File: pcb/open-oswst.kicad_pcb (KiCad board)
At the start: 2 copper layers, 70 x 50 mm, 16 parts

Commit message: PCB: standardize all JST connectors on 2mm PH pitch
SPK was JST-ZH (1.5mm); now JST-PH (2.0mm) like all others.
Increased CHNL→SPK spacing to 10mm to fit wider housing.
Removed unused add_jst_sh and add_jst_zh from kicad.py.

Co-Authored-By: Claude Opus 4.6 <noreply@anthropic.com>
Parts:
- removed the SPK at (172.0, 118.0)
- added SPK: , JST_PH_B2B, F.Cu at (175.0, 118.0)
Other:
- board text added: "open-oswst 5c44884"
- board text removed: "open-oswst cabc854"
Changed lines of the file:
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@@
   )
   (gr_rect (start 113 113) (end 183 163) (stroke (width 0.1) (type solid)) (fill none) (layer "Edge.Cuts"))
-  (gr_text "open-oswst  cabc854"
+  (gr_text "open-oswst  5c44884"
     (at 148.0 161)
     (layer "F.SilkS")
@@
     )
   )
-  (footprint "JST_ZH_B2B"
-    (layer "F.Cu")
-    (at 172 118)
+  (footprint "JST_PH_B2B"
+    (layer "F.Cu")
+    (at 175 118)
     (fp_text reference "SPK" (at 0 -2.5) (layer "F.SilkS")
       (effects (font (size 1 1) (thickness 0.15)))
     )
     (pad "-" thru_hole circle
-      (at -0.75 0)
-      (size 1.1 1.1)
-      (drill 0.7)
+      (at -1.0 0)
+      (size 1.5 1.5)
+      (drill 0.8)
       (layers *.Cu *.Mask)
       (net 11 "SPK-")
     )
     (pad "+" thru_hole circle
-      (at 0.75 0)
-      (size 1.1 1.1)
-      (drill 0.7)
+      (at 1.0 0)
+      (size 1.5 1.5)
+      (drill 0.8)
       (layers *.Cu *.Mask)
       (net 12 "SPK+")

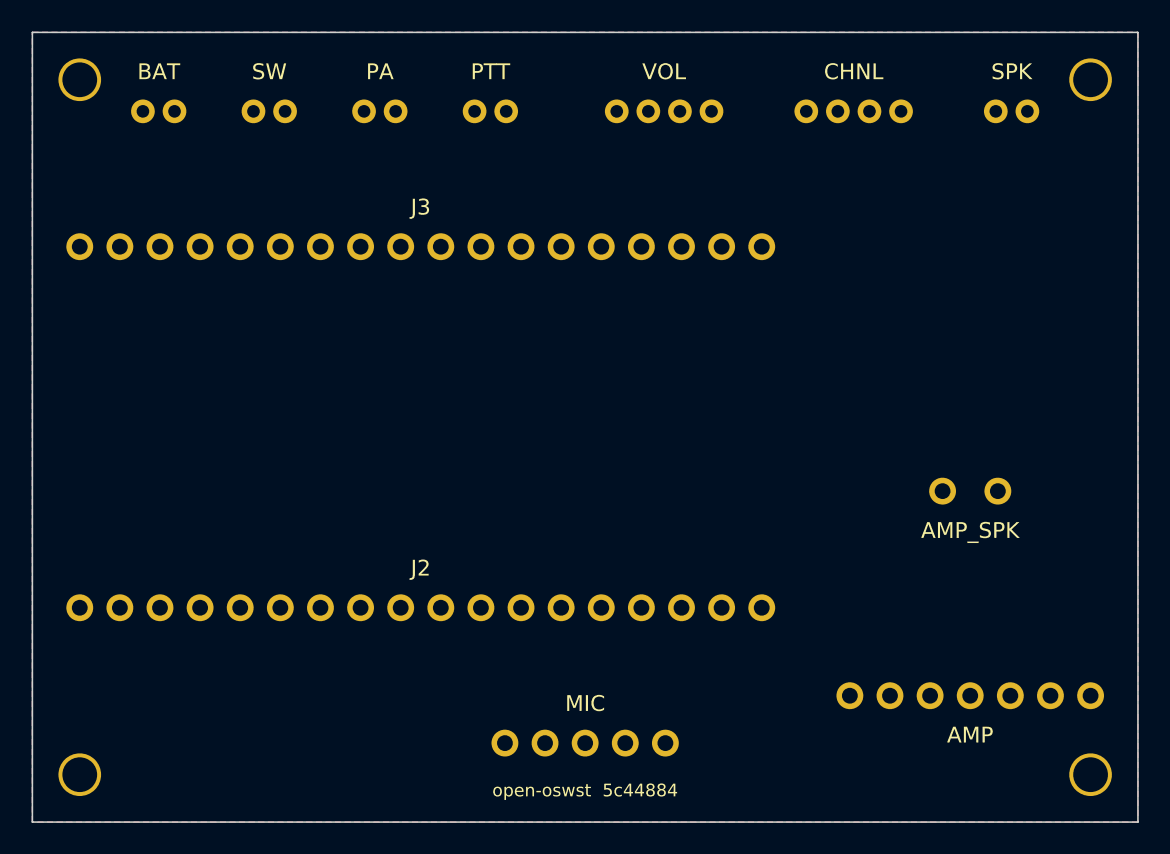
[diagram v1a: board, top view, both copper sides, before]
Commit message: PCB: match drill holes to case, relayout top connectors, move SPK to right edge
Mounting holes changed from 3mm uniform inset to 5mm LR / 2.5mm TB to
match existing case perfboard posts (60x45mm pattern). Top-edge connectors
shifted right and tightened (PTT→VOL 10mm, VOL→CHNL 11mm). SPK moved to
right edge (rotated 90°) to free space. Removed unused JST-SH/ZH methods.

Co-Authored-By: Claude Opus 4.6 <noreply@anthropic.com>
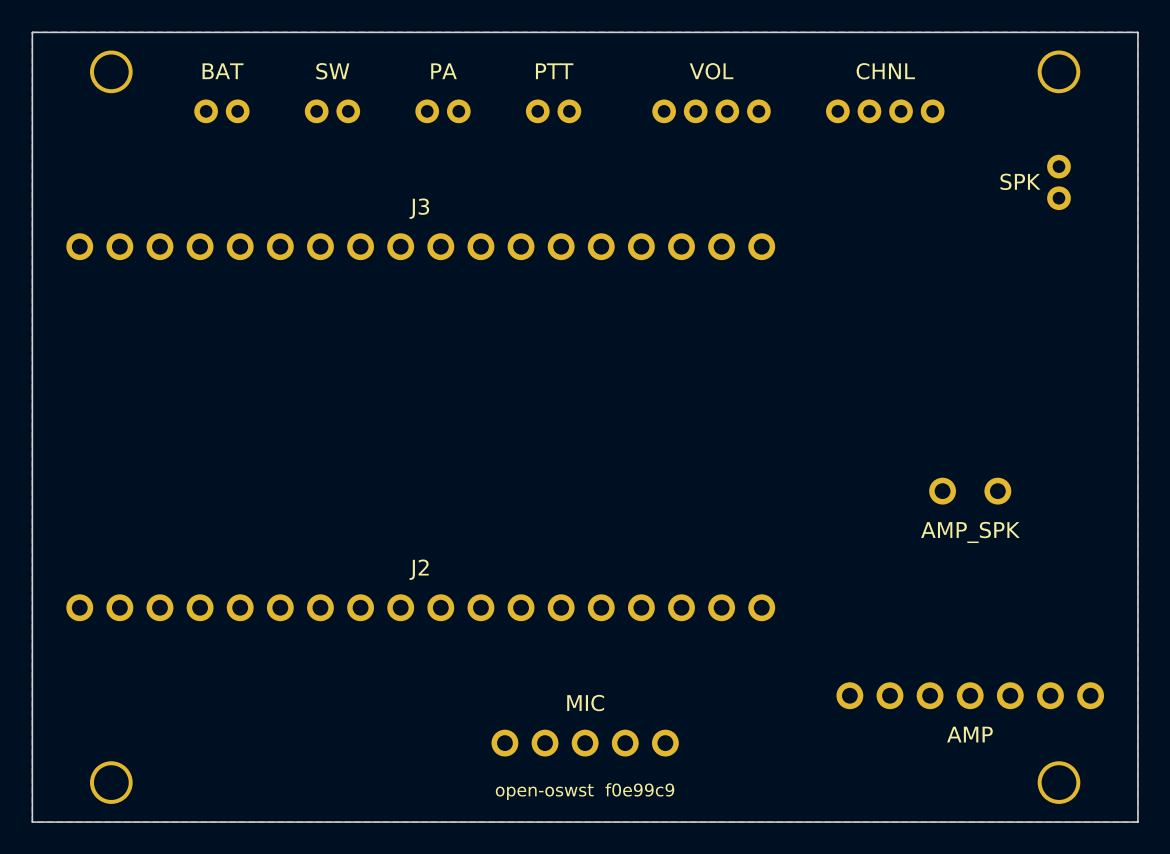
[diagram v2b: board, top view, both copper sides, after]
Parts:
- moved SPK 5.41 mm to (178.0, 122.5), turned to 90 degrees
- moved BAT 4.00 mm to (125.0, 118.0)
- moved PA 4.00 mm to (139.0, 118.0)
- moved PTT 4.00 mm to (146.0, 118.0)
- moved SW 4.00 mm to (132.0, 118.0)
- moved VOL 3.00 mm to (156.0, 118.0)
- moved H1 2.06 mm to (118.0, 115.5)
- moved H2 2.06 mm to (118.0, 160.5)
- moved H3 2.06 mm to (178.0, 115.5)
- moved H4 2.06 mm to (178.0, 160.5)
- moved CHNL 2.00 mm to (167.0, 118.0)
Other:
- board text added: "open-oswst f0e99c9"
- board text removed: "open-oswst 5c44884"
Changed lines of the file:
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@@
   )
   (gr_rect (start 113 113) (end 183 163) (stroke (width 0.1) (type solid)) (fill none) (layer "Edge.Cuts"))
-  (gr_text "open-oswst  5c44884"
+  (gr_text "open-oswst  f0e99c9"
     (at 148.0 161)
     (layer "F.SilkS")
@@
   (footprint "MountingHole_2.2mm"
     (layer "F.Cu")
-    (at 116 116)
+    (at 118 115.5)
     (attr exclude_from_pos_files exclude_from_bom)
     (fp_text reference "H1" (at 0 0) (layer "F.SilkS") hide
@@
   (footprint "MountingHole_2.2mm"
     (layer "F.Cu")
-    (at 116 160)
+    (at 118 160.5)
     (attr exclude_from_pos_files exclude_from_bom)
     (fp_text reference "H2" (at 0 0) (layer "F.SilkS") hide
@@
   (footprint "MountingHole_2.2mm"
     (layer "F.Cu")
-    (at 180 116)
+    (at 178 115.5)
     (attr exclude_from_pos_files exclude_from_bom)
     (fp_text reference "H3" (at 0 0) (layer "F.SilkS") hide
@@
   (footprint "MountingHole_2.2mm"
     (layer "F.Cu")
-    (at 180 160)
+    (at 178 160.5)
     (attr exclude_from_pos_files exclude_from_bom)
     (fp_text reference "H4" (at 0 0) (layer "F.SilkS") hide
@@
   (footprint "JST_PH_B2B"
     (layer "F.Cu")
-    (at 121 118)
+    (at 125 118)
     (fp_text reference "BAT" (at 0 -2.5) (layer "F.SilkS")
       (effects (font (size 1 1) (thickness 0.15)))
@@
   (footprint "JST_PH_B2B"
     (layer "F.Cu")
-    (at 128 118)
+    (at 132 118)
     (fp_text reference "SW" (at 0 -2.5) (layer "F.SilkS")
       (effects (font (size 1 1) (thickness 0.15)))
@@
   (footprint "JST_PH_B2B"
     (layer "F.Cu")
-    (at 135 118)
+    (at 139 118)
     (fp_text reference "PA" (at 0 -2.5) (layer "F.SilkS")
       (effects (font (size 1 1) (thickness 0.15)))
@@
   (footprint "JST_PH_B2B"
     (layer "F.Cu")
-    (at 142 118)
+    (at 146 118)
     (fp_text reference "PTT" (at 0 -2.5) (layer "F.SilkS")
       (effects (font (size 1 1) (thickness 0.15)))
@@
   (footprint "JST_PH_B4B"
     (layer "F.Cu")
-    (at 153 118)
+    (at 156 118)
     (fp_text reference "VOL" (at 0 -2.5) (layer "F.SilkS")
       (effects (font (size 1 1) (thickness 0.15)))
@@
   (footprint "JST_PH_B4B"
     (layer "F.Cu")
-    (at 165 118)
+    (at 167 118)
     (fp_text reference "CHNL" (at 0 -2.5) (layer "F.SilkS")
       (effects (font (size 1 1) (thickness 0.15)))
@@
   (footprint "JST_PH_B2B"
     (layer "F.Cu")
-    (at 175 118)
+    (at 178 122.5 90)
     (fp_text reference "SPK" (at 0 -2.5) (layer "F.SilkS")
       (effects (font (size 1 1) (thickness 0.15)))
